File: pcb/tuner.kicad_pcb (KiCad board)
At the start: 2 copper layers, 89 x 24.5 mm, 39 parts, among them P1 PDI, SW1 SPST, SW2 <, SW3 >, SW4 Mode, U1 TPS62240, U2 NKR131SB, U3 ATXMEGA8E5, Y1 8 MHz

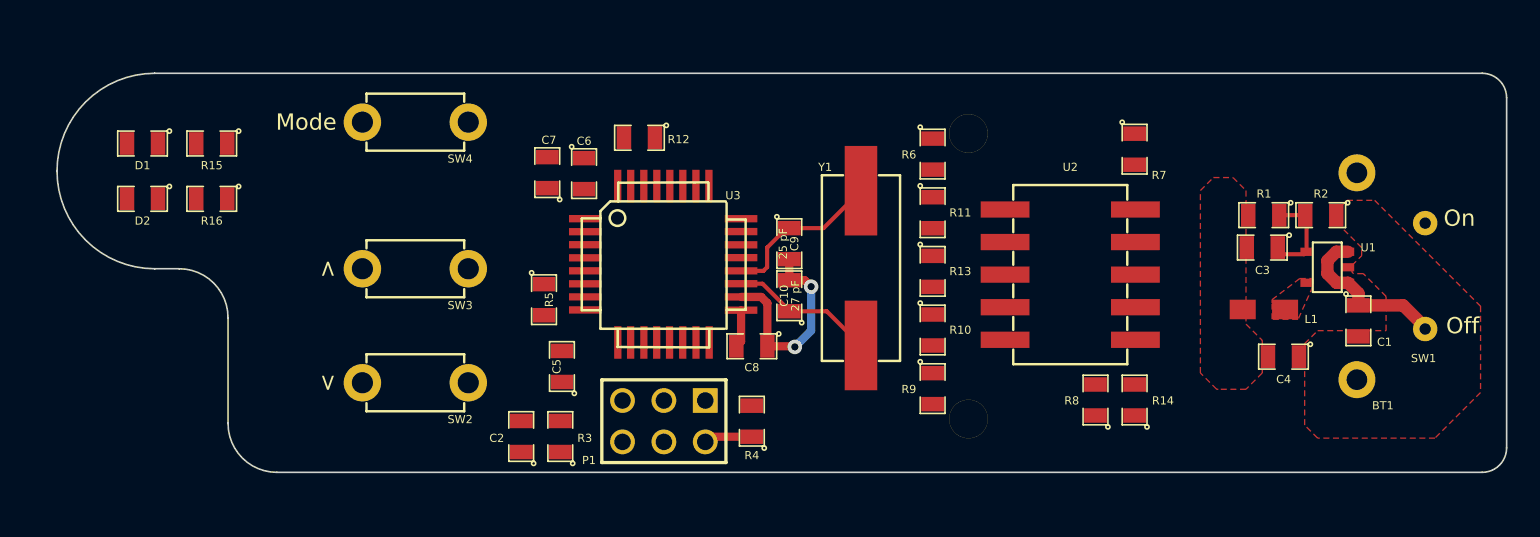
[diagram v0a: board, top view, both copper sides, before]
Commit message: - Generated traces - Changed battery holder mounting holes to non-plated through holes and modified the drill file accordingly. - Re-generated output files.
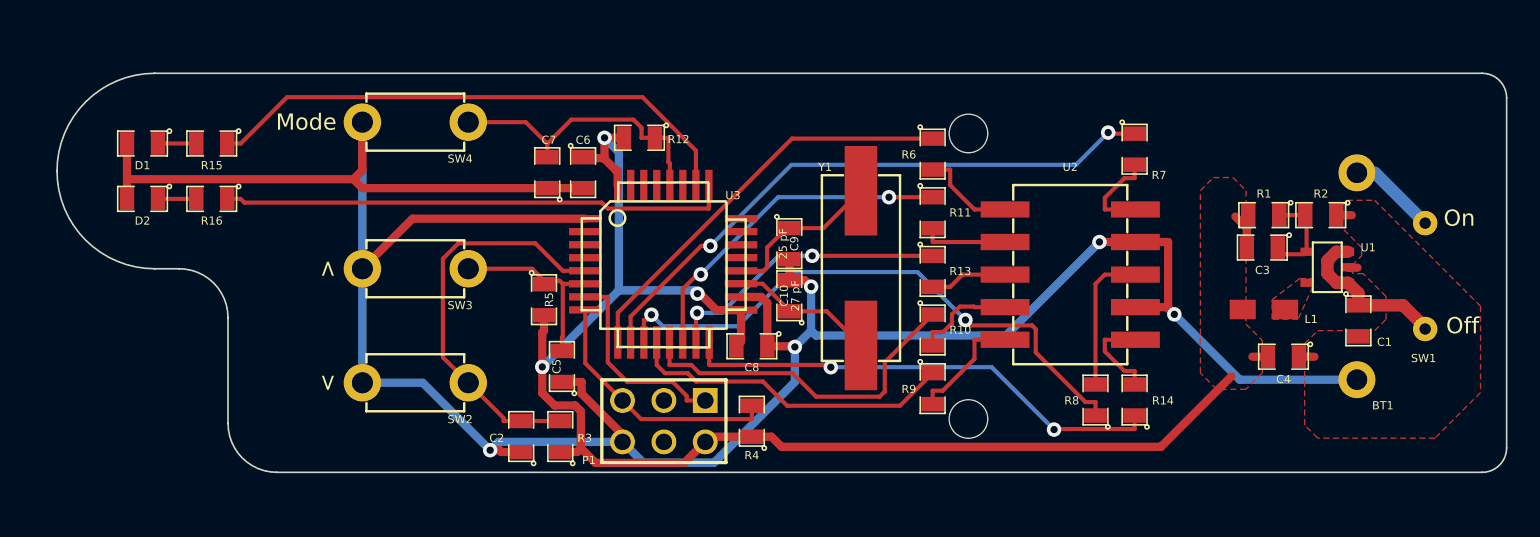
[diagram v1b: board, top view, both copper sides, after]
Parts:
- moved C6 0.08 mm to (106.3, 60.1)
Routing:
- net GND: track 13.0 -> 166.8 mm, vias 2 -> 5
- net VDD: track 5.33 -> 90.8 mm, vias 0 -> 3
- net N-000001: track 0.00 -> 37.2 mm, vias 0 -> 2
- net N-000005: track 0.00 -> 35.9 mm, vias 0 -> 2
- net N-0000011: track 0.00 -> 33.5 mm
- net N-0000010: track 0.00 -> 31.2 mm
- net N-0000013: track 0.00 -> 30.0 mm, vias 0 -> 2
- net N-000006: track 0.00 -> 25.6 mm
- net N-0000023: track 0.00 -> 24.8 mm
- net N-000003: track 0.00 -> 21.5 mm
- net N-000002: track 0.00 -> 21.0 mm, vias 0 -> 2
- net N-000004: track 0.00 -> 20.2 mm
- net N-0000033: track 0.00 -> 18.1 mm
- net N-0000014: track 0.00 -> 17.8 mm, vias 0 -> 2
- net N-0000025: track 0.00 -> 15.7 mm
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
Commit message: Rearranged layout to be more compact, reduced board length.
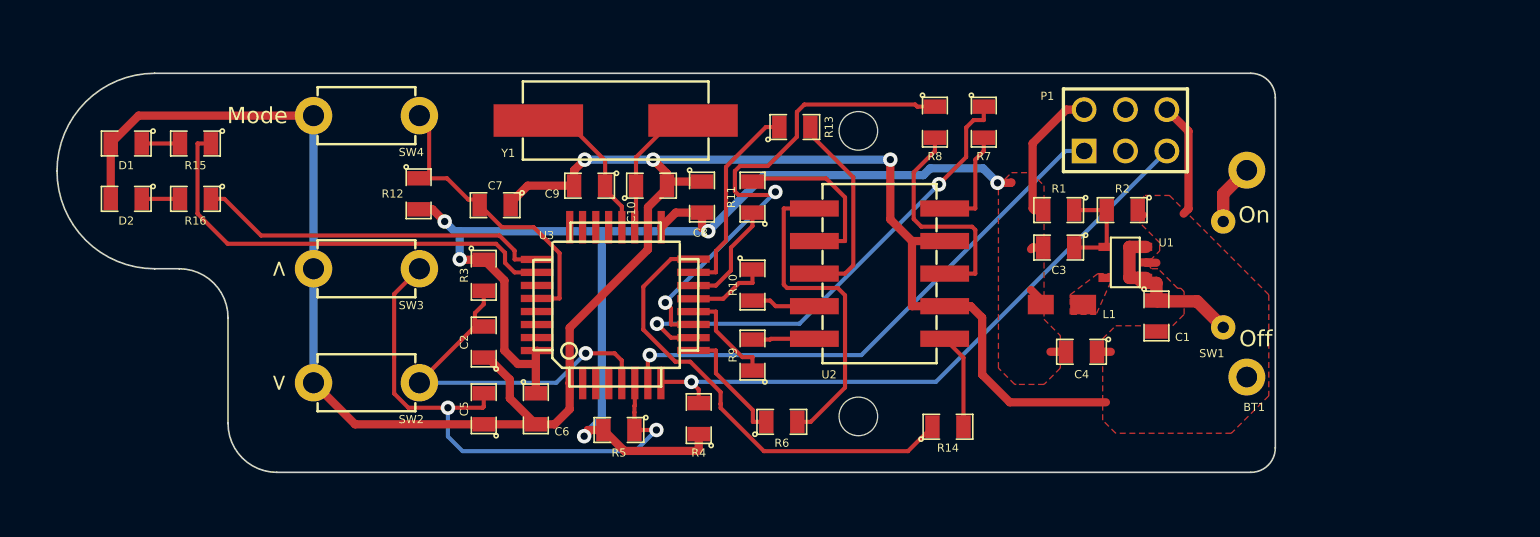
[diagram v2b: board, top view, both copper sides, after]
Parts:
- moved P1 33.5 mm to (139.6, 57.5), turned to 0 degrees
- moved R8 19.7 mm to (127.9, 57.0), turned to 270 degrees
- moved R6 18.9 mm to (118.5, 75.4), turned to 0 degrees
- moved Y1 17.6 mm to (108.3, 56.9), turned to 180 degrees
- moved C6 14.8 mm to (103.4, 74.6)
- moved R12 14.0 mm to (96.2, 61.4), turned to 270 degrees
- moved C9 12.8 mm to (106.7, 60.9), turned to 180 degrees
- moved R1 12.6 mm to (135.5, 62.4)
- moved C3 12.5 mm to (135.5, 64.7)
- moved C1 12.4 mm to (141.5, 68.9)
- moved C4 12.4 mm to (136.9, 71.1)
- moved L1 12.4 mm to (135.7, 68.2)
- moved U1 12.4 mm to (139.6, 65.6)
- moved SW1 12.4 mm to (145.6, 66.1)
- moved R13 12.3 mm to (119.3, 57.3), turned to 0 degrees
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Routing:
- net GND: track 166.8 -> 138.2 mm, vias 5 -> 3
- net N-0000024: track 11.9 -> 34.7 mm, vias 0 -> 2
- net N-0000025: track 15.7 -> 38.5 mm, vias 0 -> 1
- net N-0000026: track 12.5 -> 33.6 mm, vias 0 -> 1
- net N-000006: track 25.6 -> 7.53 mm
- net N-000003: track 21.5 -> 4.85 mm
- net N-000002: track 21.0 -> 6.79 mm, vias 2 -> 0
- net N-0000015: track 6.03 -> 20.1 mm
- net N-000004: track 20.2 -> 6.29 mm
- net N-0000010: track 31.2 -> 21.9 mm
- net N-000001: track 37.2 -> 29.7 mm
- net N-000008: track 4.76 -> 12.2 mm
- net N-0000011: track 33.5 -> 27.8 mm
- net N-0000018: track 5.28 -> 10.8 mm
- net N-0000014: track 17.8 -> 12.4 mm, vias 2 -> 0
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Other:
- board size 89 x 24.5 mm -> 74.8 x 24.5 mm

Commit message: Swapped the LEDs to avoid crossing wires, tweaked some stuff, added a ground plane.
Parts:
- moved R16 3.41 mm to (82.4, 58.3)
- moved D2 3.41 mm to (78.3, 58.3)
- moved R15 3.39 mm to (82.4, 61.7)
- moved D1 3.39 mm to (78.3, 61.7)
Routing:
- net GND: track 138.2 -> 27.0 mm, vias 3 -> 8
- net VDD: track 90.9 -> 77.3 mm, vias 5 -> 6
- net N-000001: track 29.7 -> 42.8 mm, vias 2 -> 0
- net N-0000025: track 38.5 -> 51.5 mm, vias 1 -> 0
- net N-0000026: track 33.6 -> 46.0 mm, vias 1 -> 2
- net N-0000013: track 28.5 -> 19.7 mm, vias 0 -> 2
- net N-0000011: track 27.8 -> 22.0 mm
- net N-0000024: track 34.7 -> 31.0 mm, vias 2 -> 0
- net N-000005: track 31.3 -> 28.1 mm, vias 2 -> 0
- net N-0000020: track 14.2 -> 11.7 mm
- net N-000007: track 5.88 -> 7.58 mm
- net N-0000023: track 22.6 -> 21.1 mm, vias 1 -> 0
- net N-0000010: track 21.9 -> 23.1 mm
- net N-0000031: track 10.3 -> 9.64 mm
- net N-0000033: track 19.8 -> 19.2 mm
- added copper zone on B.Cu, net GND

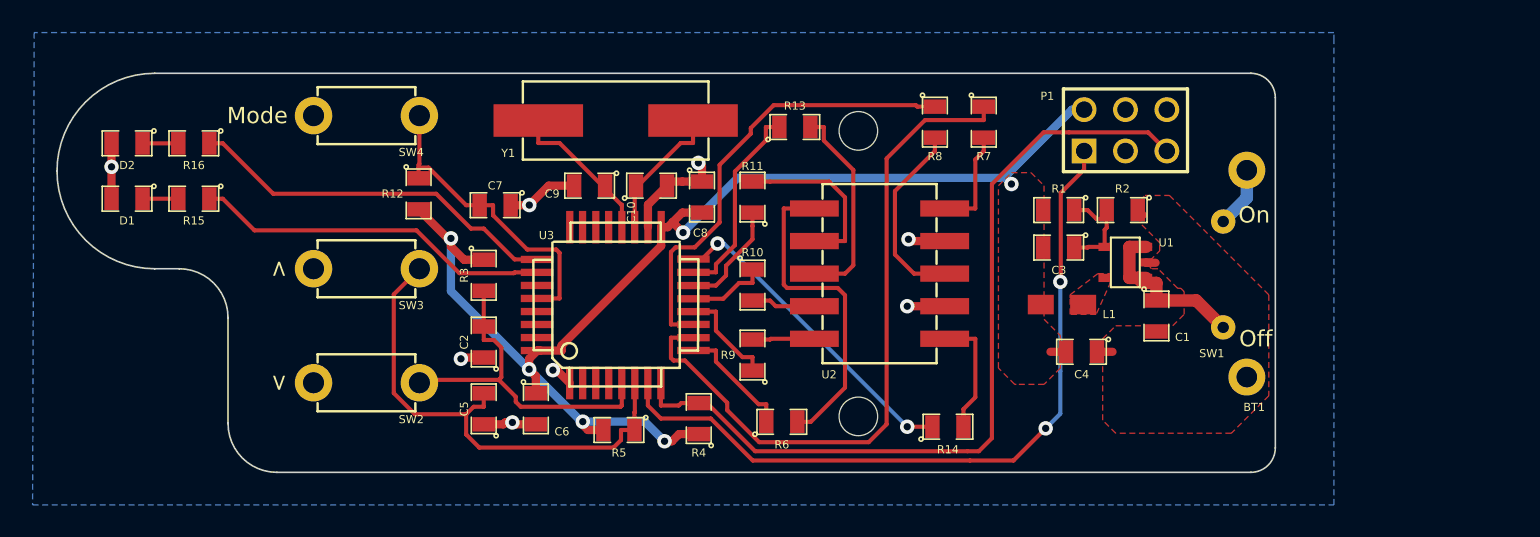
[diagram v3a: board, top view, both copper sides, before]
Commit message: Final tweaks to PCB layout, added CC BY-SA license.  This commit corresponds to the initial PCB run.
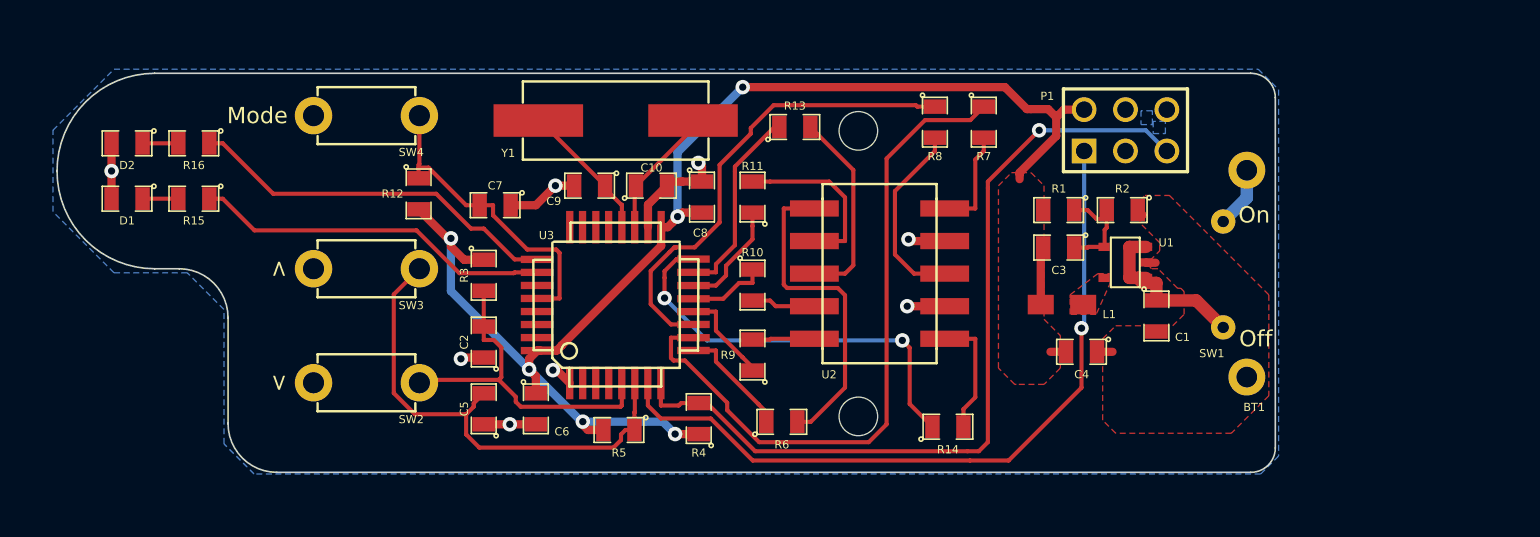
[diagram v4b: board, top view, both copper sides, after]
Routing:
- net VDD: track 77.3 -> 87.6 mm
- net N-0000013: track 19.7 -> 26.0 mm
- net N-000005: track 28.1 -> 29.2 mm
- net N-0000031: track 9.64 -> 9.01 mm
- net N-0000024: track 31.0 -> 30.5 mm
- net N-0000025: track 51.5 -> 51.8 mm, vias 0 -> 1
- net N-0000026: track 46.0 -> 45.9 mm, vias 2 -> 1
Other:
- board text added: "CC BY-SA License: http://creativecommons.org/licenses/by-sa/4.0/legalcode"
- board text added: "Strobe Guitar Tuner r2 http://nrqm.ca/tuner/ CC BY-SA 4.0"
- board text removed: "© 2014 Neil MacMillan Strobe Guitar Tuner r2 http://nrqm.ca/guitar-tuner"
